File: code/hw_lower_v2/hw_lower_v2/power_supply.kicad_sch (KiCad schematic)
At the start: 32 parts, among them J10 Conn_01x02, J11 Conn_01x02, J12 Conn_01x02, J13 Conn_01x02, J14 Conn_01x02, J9 Conn_01x02, U5 ICL7660A, U6 AMS1117, U7 AMS1117

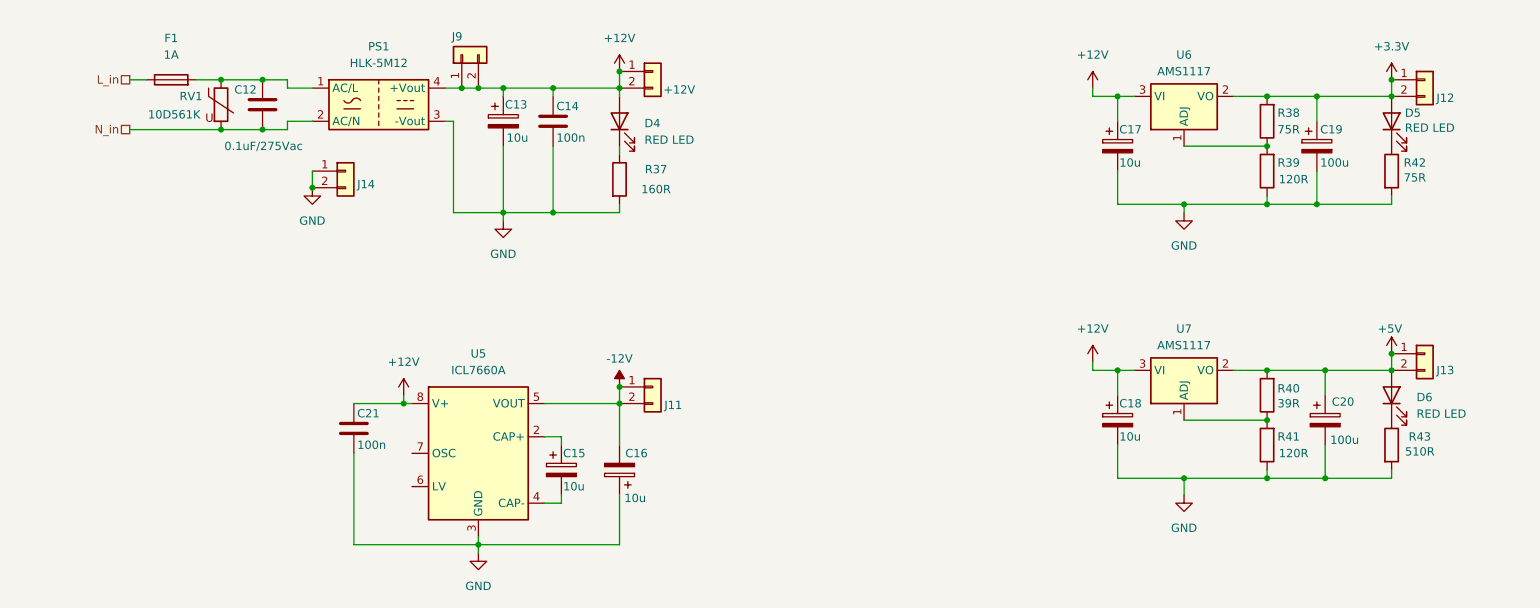
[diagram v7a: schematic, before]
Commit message: switch power  pin headers for jumpers
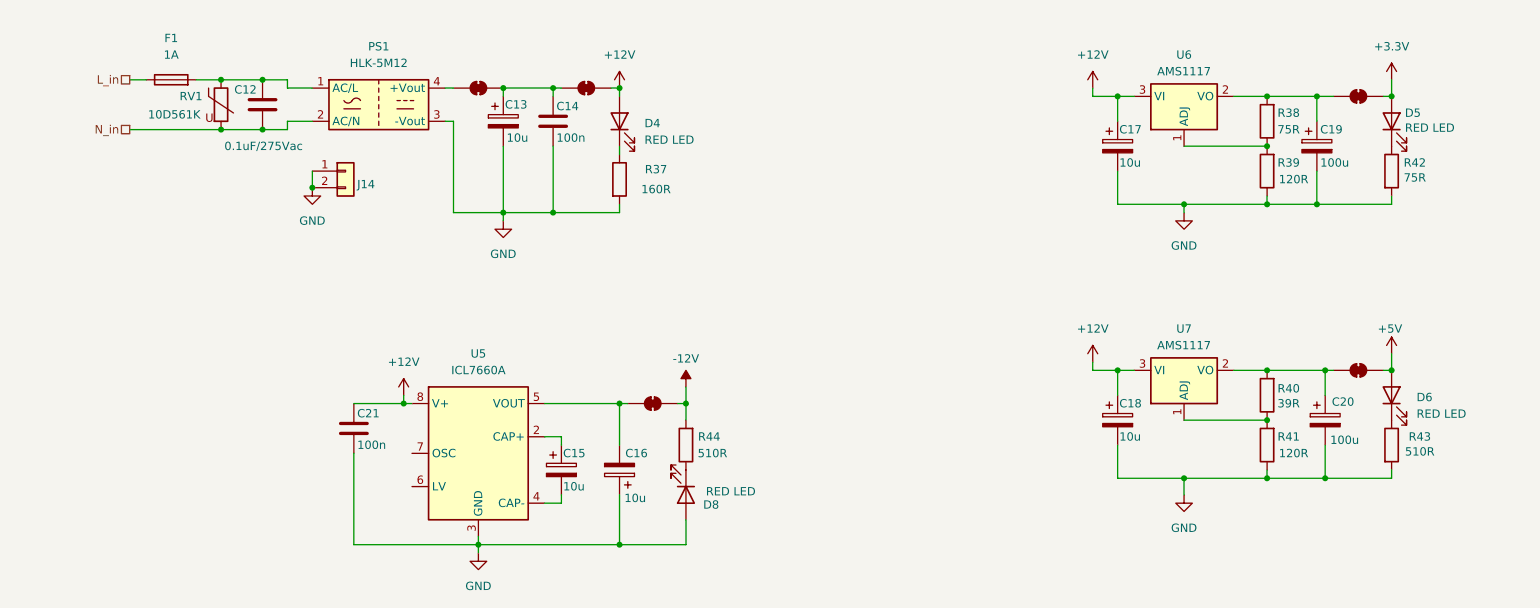
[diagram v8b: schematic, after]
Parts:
- removed J10, J11, J12, J13, J9: Conn_01x02, Connector_PinHeader_2.54mm:PinHeader_1x02_P2.54mm_Vertical, symbol Connector_Generic:Conn_01x02
- added D8: RED LED, Diode_SMD:D_0603_1608Metric, symbol Device:LED
- added JP1, JP2, JP3, JP4, JP5: SolderJumper_2_Bridged, Jumper:SolderJumper-2_P1.3mm_Bridged2Bar_RoundedPad1.0x1.5mm, symbol Jumper:SolderJumper_2_Bridged
- added R44: 510R, Resistor_SMD:R_0603_1608Metric, symbol Device:R
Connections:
- net +12V: now also JP1.1 (A); no longer C13.1, C14.1, PS1.4 (+Vout)
- net +3.3V: now also JP4.1 (A); no longer C19.1, R38.2, U6.2 (VO)
- net +5V: now also JP5.1 (A); no longer C20.1, R40.2, U7.2 (VO)
- net -12V: now also JP3.1 (A), R44.2; no longer C16.2, U5.5 (VOUT)
- net GND: now also D8.2 (A)
- new net: D8.1 (K), R44.1
- new net: C19.1, JP4.2 (B), R38.2, U6.2 (VO)
- new net: C13.1, C14.1, JP1.2 (B), JP2.1 (A)
- new net: C16.2, JP3.2 (B), U5.5 (VOUT)
- new net: C20.1, JP5.2 (B), R40.2, U7.2 (VO)
- new net: JP2.2 (B), PS1.4 (+Vout)
